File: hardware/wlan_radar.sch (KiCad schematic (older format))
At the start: 103 parts, among them P1 CONN_2, P2 CONN_2, Q1 MOS_P_BSS84, U1 SST11LP12, U10 LTC6242, U11 LT6230, U12 MCP4017, U15 TSV321RAILT, U16 LM2681, U17 TSV321RAILT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

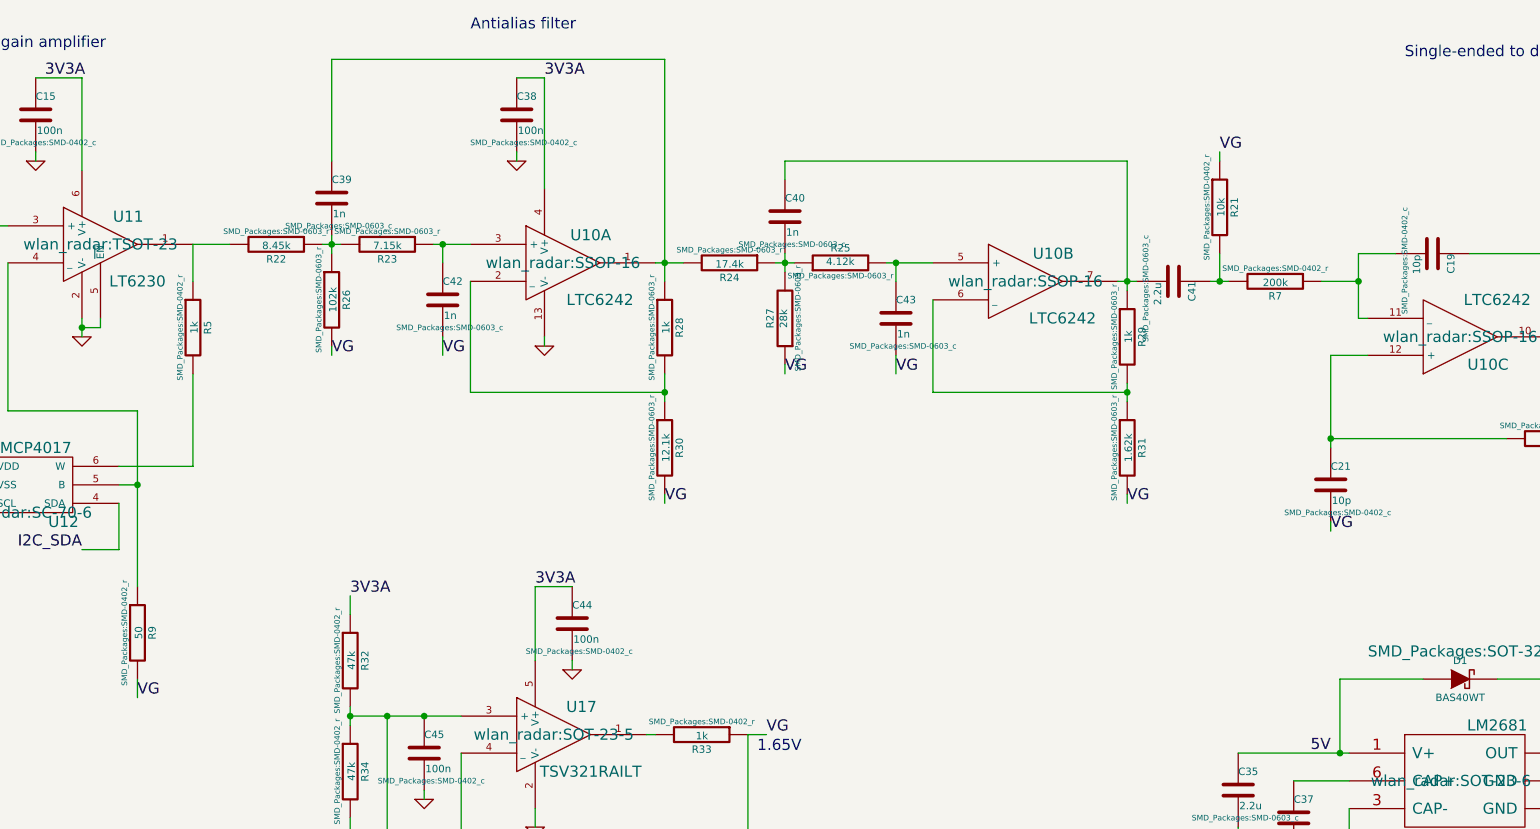
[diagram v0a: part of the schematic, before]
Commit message: Fix hardware mistakes
This commit adds fixes some of the mistakes identified after the
board was ordered.

Add 100n capacitor to MCUs reset pin to fix programming issues.

Add series connection of resistor and capacitor in parallel
with mixer output amplifier to fix the DC balance issue.

Remove the now unneeded capacitor and resistor
after the low-pass filter.

Add 200k resistor in feedback path of single-ended to differential
conversion circuit to solve the issue with limited input voltage range.
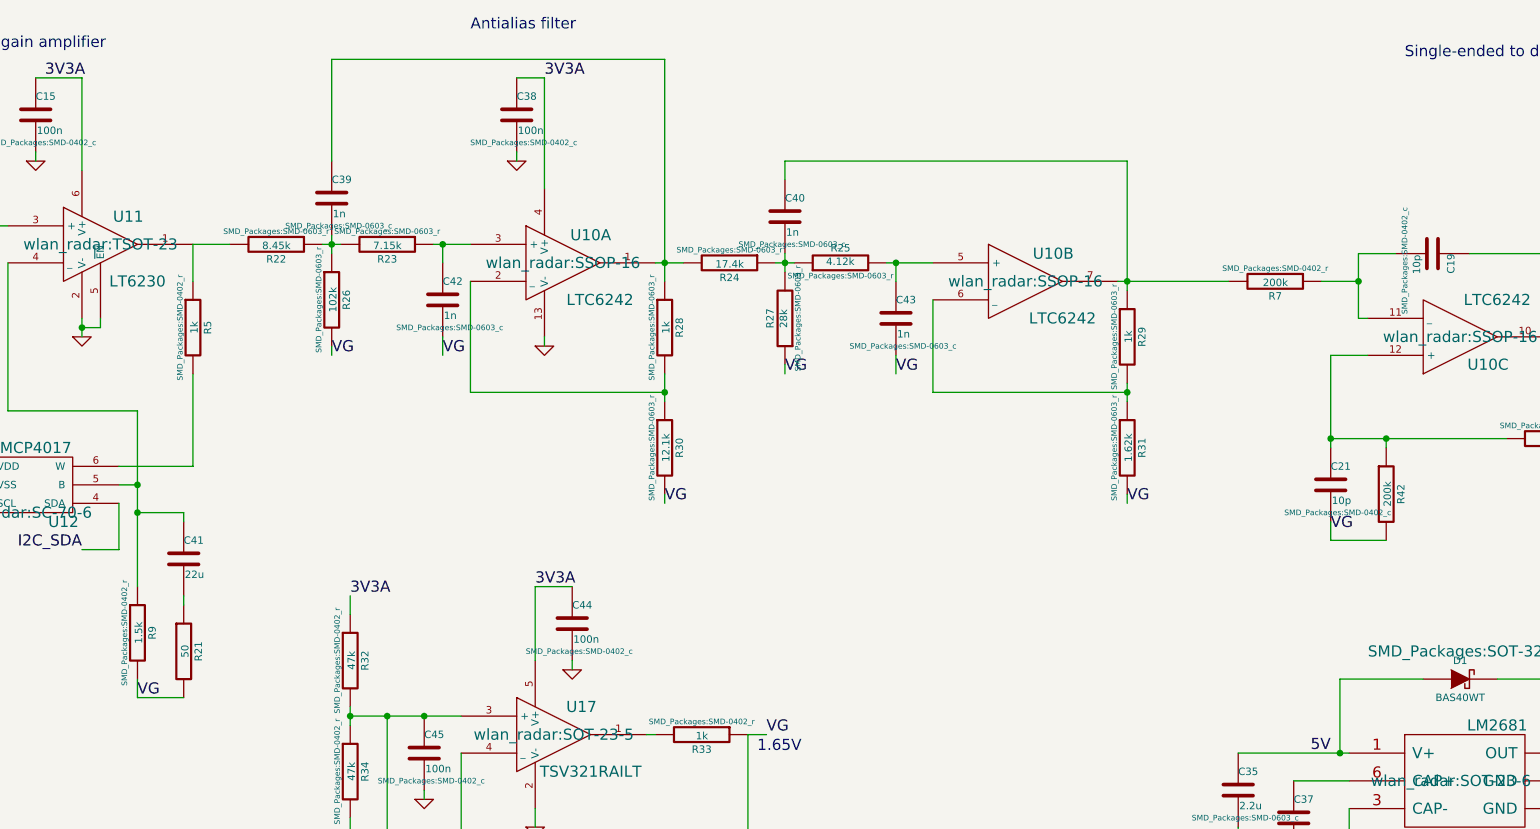
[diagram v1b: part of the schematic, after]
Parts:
- added R42: 200k, SMD_Packages:SMD-0402_r, symbol R
- C41: value 2.2u -> 22u; footprint SMD_Packages:SMD-0603_c -> SMD_Packages:SMD-0805
- R21: value 10k -> 50
- R9: value 50 -> 1.5k
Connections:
- net VG: now also R21.2, R42.2; no longer R21.1
- net at R9.1, U11.4 (_), U12.5 (B): now also C41.1
- net at C40.1, R29.1, U10.7: now also R7.2; no longer C41.2
- net at C21.1, R8.2, U10.12 (+): now also R42.1
- new net: C41.2, R21.1
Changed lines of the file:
@@
 LIBS:valves
 LIBS:wlan_radar
-LIBS:sam_board
 LIBS:wlan_radar-cache
 EELAYER 25 0
@@
 P 2550 9100
 F 0 "R9" V 2630 9100 40  0000 C CNN
-F 1 "50" V 2557 9101 40  0000 C CNN
+F 1 "1.5k" V 2557 9101 40  0000 C CNN
 F 2 "SMD_Packages:SMD-0402_r" V 2480 9100 30  0000 C CNN
 F 3 "" H 2550 9100 30  0000 C CNN
@@
 VG
 $Comp
-L C C41
-U 1 1 53F404D2
-P 8150 7200
-F 0 "C41" H 8150 7300 40  0000 L CNN
-F 1 "2.2u" H 8156 7115 40  0000 L CNN
-F 2 "SMD_Packages:SMD-0603_c" H 8188 7050 30  0000 C CNN
-F 3 "" H 8150 7200 60  0000 C CNN
-	1    8150 7200
-	0    1    1    0
-$EndComp
-$Comp
-L R R21
-U 1 1 53F40576
-P 8400 6800
-F 0 "R21" V 8480 6800 40  0000 C CNN
-F 1 "10k" V 8407 6801 40  0000 C CNN
-F 2 "SMD_Packages:SMD-0402_r" V 8330 6800 30  0000 C CNN
-F 3 "" H 8400 6800 30  0000 C CNN
-	1    8400 6800
-	1    0    0    -1
-$EndComp
-Text Label 8400 6500 0    60   ~ 0
-VG
-$Comp
 L R R35
 U 1 1 53F436C6
@@
 Connection ~ 9000 8050
 Wire Wire Line
-	9000 8500 9000 8550
+	9000 8500 9000 8600
 Wire Wire Line
 	2350 7400 2350 7450
@@
 Connection ~ 7900 7800
 Wire Wire Line
-	7850 7200 7950 7200
+	7850 7200 8450 7200
 Wire Wire Line
 	7900 6550 7900 7250
 Wire Wire Line
 	7900 8350 7900 8400
-Wire Wire Line
-	8350 7200 8450 7200
 Connection ~ 7900 7200
-Wire Wire Line
-	8400 7050 8400 7200
-Connection ~ 8400 7200
-Wire Wire Line
-	8400 6550 8400 6500
 Wire Wire Line
 	3900 9550 3900 10550
@@
 Wire Wire Line
 	14900 6650 15000 6650
+$Comp
+L C C41
+U 1 1 5480D4BB
+P 2800 8700
+F 0 "C41" H 2800 8800 40  0000 L CNN
+F 1 "22u" H 2806 8615 40  0000 L CNN
+F 2 "SMD_Packages:SMD-0805" H 2838 8550 30  0001 C CNN
+F 3 "" H 2800 8700 60  0000 C CNN
+	1    2800 8700
+	1    0    0    -1
+$EndComp
+$Comp
+L R R21
+U 1 1 5480D563
+P 2800 9200
+F 0 "R21" V 2880 9200 40  0000 C CNN
+F 1 "50" V 2807 9201 40  0000 C CNN
+F 2 "SMD_Packages:SMD-0402_r" V 2730 9200 30  0001 C CNN
+F 3 "" H 2800 9200 30  0000 C CNN
+	1    2800 9200
+	1    0    0    -1
+$EndComp
+Wire Wire Line
+	2550 9450 2800 9450
+Wire Wire Line
+	2800 8500 2800 8450
+Wire Wire Line
+	2800 8450 2550 8450
+Connection ~ 2550 8450
+Wire Wire Line
+	2800 8900 2800 8950
+$Comp
+L R R42
+U 1 1 5480D381
+P 9300 8350
+F 0 "R42" V 9380 8350 40  0000 C CNN
+F 1 "200k" V 9307 8351 40  0000 C CNN
+F 2 "SMD_Packages:SMD-0402_r" V 9230 8350 30  0001 C CNN
+F 3 "" H 9300 8350 30  0000 C CNN
+	1    9300 8350
+	1    0    0    -1
+$EndComp
+Wire Wire Line
+	9300 8050 9300 8100
+Connection ~ 9300 8050
+Wire Wire Line
+	9000 8600 9300 8600
 $EndSCHEMATC
